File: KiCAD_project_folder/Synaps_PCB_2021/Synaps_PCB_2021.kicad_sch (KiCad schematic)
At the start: 0 parts

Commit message: Update schematic sheets and creates image to allow the board setup to be shared
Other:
- company: (none) -> Club SynapsÉTS
- title: Electrode PCB -> Misca PCB
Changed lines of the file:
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@@
   (paper "A4")
   (title_block
-    (title "Electrode PCB")
-    (date "2020-12-29")
+    (title "Misca PCB")
+    (date "2022-06-17")
+    (rev "A2")
+    (company "Club SynapsÉTS")
+    (comment 1 "Auteur : Jacques Veneziano")
   )
   (wire (pts (xy 102.87 133.35) (xy 151.13 133.35))

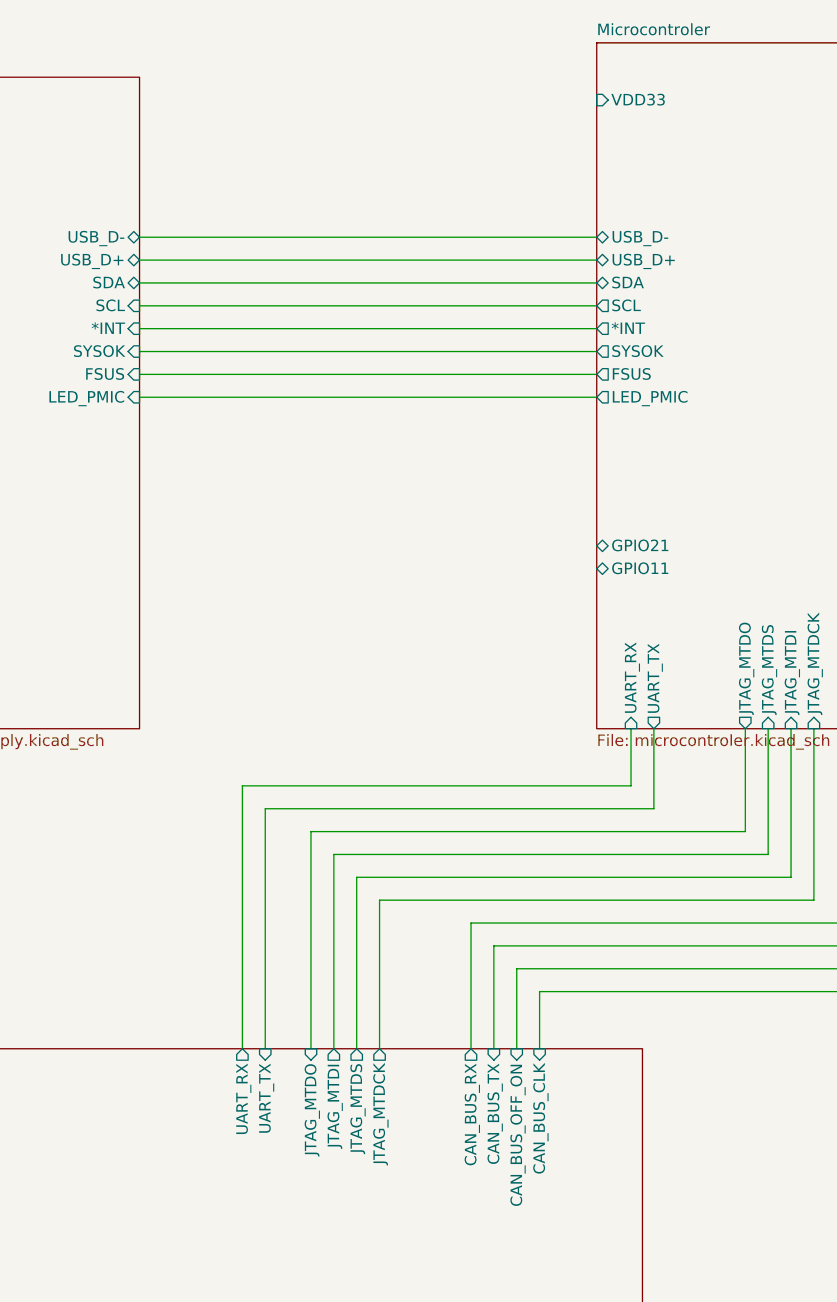
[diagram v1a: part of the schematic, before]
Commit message: Fixed missing connections + plus added rough BOM
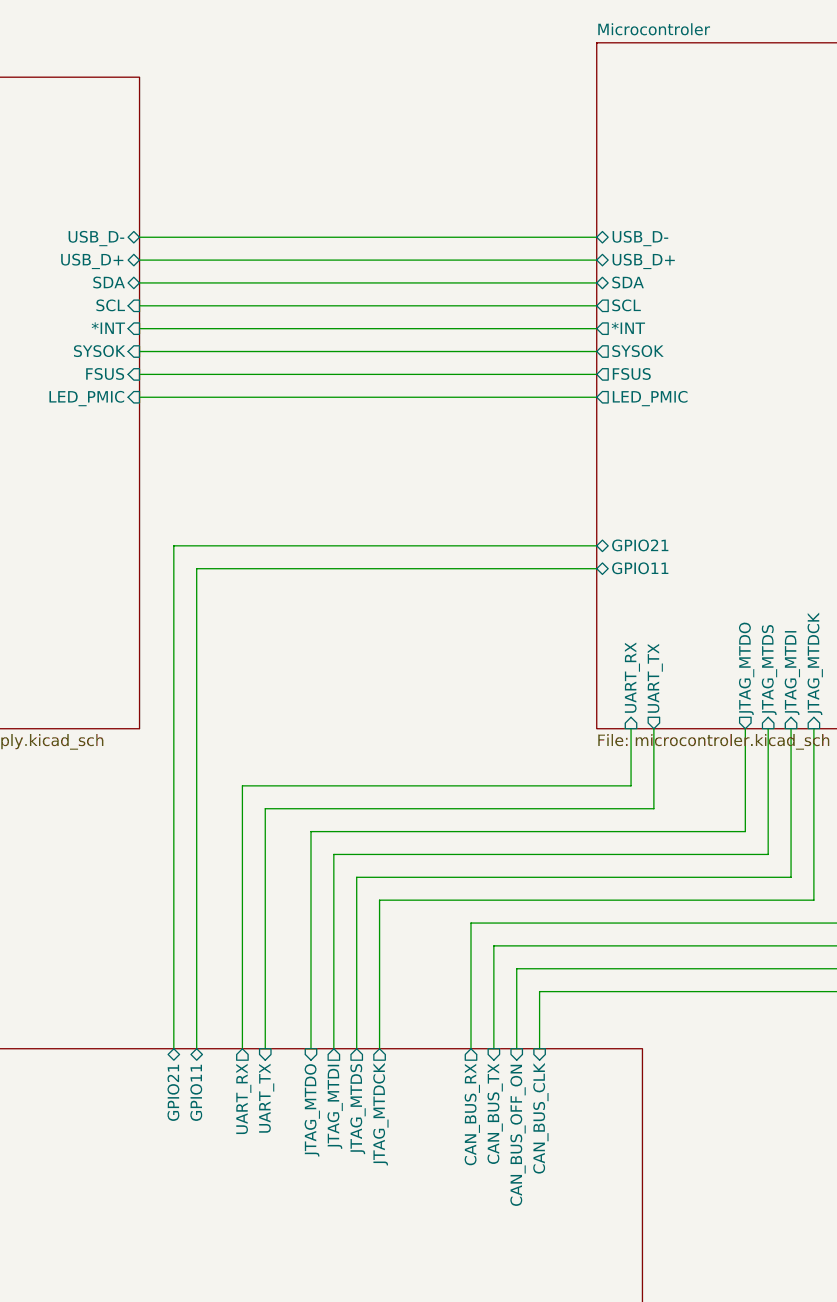
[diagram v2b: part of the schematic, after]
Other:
- sheet Connectors ports: added GPIO11, GPIO21; removed none
- sheet Microcontroler ports: added none; removed VDD33
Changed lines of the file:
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@@
+    (stroke (width 0) (type default) (color 0 0 0 0))
+  )
+  (wire (pts (xy 82.55 149.86) (xy 82.55 96.52))
     (stroke (width 0) (type default) (color 0 0 0 0))
   )
@@
     (stroke (width 0) (type default) (color 0 0 0 0))
   )
+  (wire (pts (xy 82.55 96.52) (xy 127 96.52))
+    (stroke (width 0) (type default) (color 0 0 0 0))
+  )
+  (wire (pts (xy 80.01 93.98) (xy 127 93.98))
+    (stroke (width 0) (type default) (color 0 0 0 0))
+  )
   (wire (pts (xy 102.87 149.86) (xy 102.87 133.35))
     (stroke (width 0) (type default) (color 0 0 0 0))
@@
   )
   (wire (pts (xy 190.5 55.88) (xy 223.52 55.88))
+    (stroke (width 0) (type default) (color 0 0 0 0))
+  )
+  (wire (pts (xy 80.01 149.86) (xy 80.01 93.98))
     (stroke (width 0) (type default) (color 0 0 0 0))
   )
@@
       (effects (font (size 1.27 1.27)) (justify left top))
     )
-    (pin "VDD33" input (at 127 44.45 180)
-      (effects (font (size 1.27 1.27)) (justify left))
-    )
     (pin "USB_D-" bidirectional (at 127 59.69 180)
       (effects (font (size 1.27 1.27)) (justify left))
@@
     )
     (pin "CAN_BUS_TX" input (at 115.57 149.86 90)
+      (effects (font (size 1.27 1.27)) (justify right))
+    )
+    (pin "GPIO21" bidirectional (at 80.01 149.86 90)
+      (effects (font (size 1.27 1.27)) (justify right))
+    )
+    (pin "GPIO11" bidirectional (at 82.55 149.86 90)
       (effects (font (size 1.27 1.27)) (justify right))
     )
@@
       (reference "#PWR013") (unit 1) (value "GNDREF") (footprint "")
     )
-    (path "/00000000-0000-0000-0000-0000604af200/ef1da815-5ae9-4f7a-859c-d7960e6acc1e"
-      (reference "#PWR014") (unit 1) (value "VBUS") (footprint "")
-    )
     (path "/00000000-0000-0000-0000-0000604af200/b5aba46c-977a-4706-899d-5875980faab4"
       (reference "#PWR015") (unit 1) (value "VDD") (footprint "")
@@
       (reference "#PWR048") (unit 1) (value "+3.3V") (footprint "")
     )
-    (path "/00000000-0000-0000-0000-0000604b51e6/985fc325-4e90-4701-95f1-1aa7b43358fb"
-      (reference "#PWR049") (unit 1) (value "GNDREF") (footprint "")
-    )
-    (path "/00000000-0000-0000-0000-0000604b51e6/49a828ae-3f98-4bd8-bef9-14a992299c68"
-      (reference "#PWR050") (unit 1) (value "GNDREF") (footprint "")
-    )
     (path "/00000000-0000-0000-0000-0000604b51e6/f3f572b8-a413-4bfd-9f78-f7f49ba1498c"
       (reference "#PWR051") (unit 1) (value "GNDREF") (footprint "")
@@
       (reference "#PWR075") (unit 1) (value "GNDREF") (footprint "")
     )
+    (path "/00000000-0000-0000-0000-0000604b51e6/285eee95-fe40-4a76-9ead-469d3137b903"
+      (reference "#PWR0101") (unit 1) (value "GNDREF") (footprint "")
+    )
     (path "/00000000-0000-0000-0000-0000604af200/eaf45722-852c-47af-8403-1f057ec76e15"
       (reference "#PWR0102") (unit 1) (value "GNDREF") (footprint "")
     )
+    (path "/00000000-0000-0000-0000-0000604af200/4c6a8406-b60a-4727-b2ce-f8d643541f7a"
+      (reference "#PWR0103") (unit 1) (value "VBUS") (footprint "")
+    )
     (path "/00000000-0000-0000-0000-0000604af200/29ab8ef7-d469-4192-a436-a1a2c51aa419"
       (reference "#PWR0104") (unit 1) (value "GNDREF") (footprint "")
@@
     )
     (path "/00000000-0000-0000-0000-0000604af200/30e58f79-c173-4870-9af4-7e80c241c783"
-      (reference "Q2") (unit 1) (value "Q_PMOS_DGS") (footprint "Transformer_NF_ETAL_P2781")
+      (reference "Q2") (unit 1) (value "Q_PMOS_DGS") (footprint "Transformer_SMD:Transformer_NF_ETAL_P2781")
     )
     (path "/00000000-0000-0000-0000-0000604af200/8834be57-e470-4d6f-9ac6-cbc55a7612e6"

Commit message: wip
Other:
- sheet Probes schematic ports: added *INT, SCL, SDA; removed none
